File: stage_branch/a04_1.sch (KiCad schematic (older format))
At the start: 17 parts, among them U4001 74HC02, U4002 74HC27, U4003 74LVC07, U4004 74HC27, U4005 74HC02, U4006 74HC02, U4007 74HC04, U4008 74HC04, U4009 74HC27, U4010 74HC4002, U4011 74HC02, U4012 74HC02, U4013 74HC02, U4014 74HC4002, U4015 74HC27

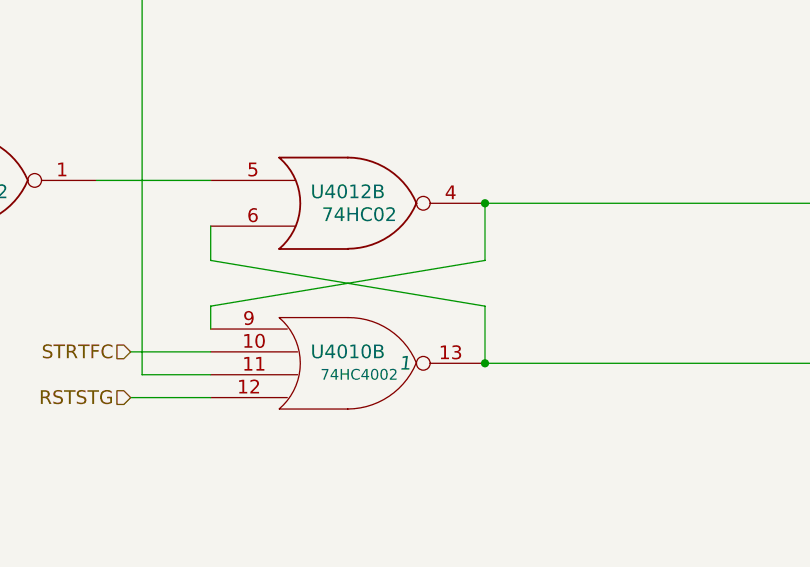
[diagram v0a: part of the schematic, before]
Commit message: More initial conditions fixes, prevents STG3 from oscillating and freqking out TC0
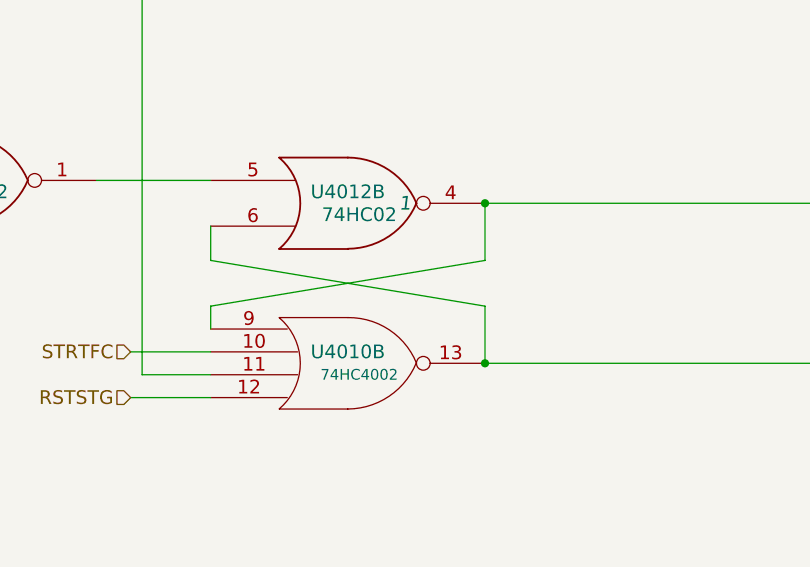
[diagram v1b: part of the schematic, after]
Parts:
- U4010: Initial 1 -> (none)
- U4012: Initial (none) -> 1
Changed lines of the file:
@@
 F 2 "" H 3850 8000 60  0000 C CNN
 F 3 "" H 3850 8000 60  0000 C CNN
-F 4 "1" H 4100 8000 60  0000 C CIN "Initial"
 	2    3850 8000
 	1    0    0    -1
@@
 F 2 "" H 3850 7300 60  0000 C CNN
 F 3 "" H 3850 7300 60  0000 C CNN
+F 4 "1" H 4100 7300 60  0000 C CIN "Initial"
 	2    3850 7300
 	1    0    0    -1

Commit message: Finished off the first page of the Stage Branch Decoding module.
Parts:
- added R2007, R3004, R3005, R4003, R4006: 5k, symbol R
- added unit 5 of U4003
- added unit 6 of U4003
- added unit 4 of U4007
- added unit 5 of U4007
- added unit 5 of U4008
- added unit 6 of U4008
- added unit 3 of U4013
- added unit 4 of U4013
- added unit 2 of U4015
- added unit 3 of U4015
- added U4016, U4018, U4019, U4021, U4024, U4030: 74HC02, symbol 74HC02
- added U4017, U4025: 74HC04, symbol 74HC04
- added U4020, U4026: 74HC27, symbol 74HC27
- added U4022, U4027, U4028: 74HC4002, symbol 74HC4002
- added U4023, U4029: 74LVC07, symbol 74LVC07
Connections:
- net GND: now also U4003.7 (GND), U4003.7 (GND), U4007.7 (GND), U4007.7 (GND), U4008.7 (GND), U4008.7 (GND), U4013.7 (GND), U4013.7 (GND), U4015.7 (GND), U4015.7 (GND), U4016.7 (GND), U4016.7 (GND), U4016.7 (GND), U4016.7 (GND), U4017.7 (GND), U4017.7 (GND), U4017.7 (GND), U4017.7 (GND), U4017.7 (GND), U4017.7 (GND), U4018.7 (GND), U4018.7 (GND), U4018.7 (GND), U4018.7 (GND), U4019.7 (GND), U4019.7 (GND), U4019.7 (GND), U4019.7 (GND), U4020.7 (GND), U4020.7 (GND), U4020.7 (GND), U4021.7 (GND), U4021.7 (GND), U4021.7 (GND), U4021.7 (GND), U4022.7 (GND), U4022.7 (GND), U4023.7 (GND), U4023.7 (GND), U4023.7 (GND), U4023.7 (GND), U4023.7 (GND), U4023.7 (GND), U4024.7 (GND), U4024.7 (GND), U4024.7 (GND), U4024.7 (GND), U4025.7 (GND), U4025.7 (GND), U4025.7 (GND), U4025.7 (GND), U4026.7 (GND), U4026.7 (GND), U4026.7 (GND), U4027.7 (GND), U4027.7 (GND), U4028.7 (GND), U4028.7 (GND), U4029.7 (GND), U4029.7 (GND), U4029.7 (GND), U4029.7 (GND), U4029.7 (GND), U4030.7 (GND), U4030.7 (GND)
- net PHS3/: now also U4019.6, U4021.3, U4021.6, U4022.3, U4024.9, U4030.3
- net ST0/: now also U4018.3
- net ST1/: now also U4018.6
- net ST4/: now also U4018.9
- net STG1: now also U4013.8
- net STG3: now also U4013.9
- net VCC: now also R2007.1, R3004.1, R3005.1, R4003.1, R4006.1, U4003.14 (VCC), U4003.14 (VCC), U4007.14 (VCC), U4007.14 (VCC), U4008.14 (VCC), U4008.14 (VCC), U4013.14 (VCC), U4013.14 (VCC), U4015.14 (VCC), U4015.14 (VCC), U4016.14 (VCC), U4016.14 (VCC), U4016.14 (VCC), U4016.14 (VCC), U4017.14 (VCC), U4017.14 (VCC), U4017.14 (VCC), U4017.14 (VCC), U4017.14 (VCC), U4017.14 (VCC), U4018.14 (VCC), U4018.14 (VCC), U4018.14 (VCC), U4018.14 (VCC), U4019.14 (VCC), U4019.14 (VCC), U4019.14 (VCC), U4019.14 (VCC), U4020.14 (VCC), U4020.14 (VCC), U4020.14 (VCC), U4021.14 (VCC), U4021.14 (VCC), U4021.14 (VCC), U4021.14 (VCC), U4022.14 (VCC), U4022.14 (VCC), U4023.14 (VCC), U4023.14 (VCC), U4023.14 (VCC), U4023.14 (VCC), U4023.14 (VCC), U4023.14 (VCC), U4024.14 (VCC), U4024.14 (VCC), U4024.14 (VCC), U4024.14 (VCC), U4025.14 (VCC), U4025.14 (VCC), U4025.14 (VCC), U4025.14 (VCC), U4026.14 (VCC), U4026.14 (VCC), U4026.14 (VCC), U4027.14 (VCC), U4027.14 (VCC), U4028.14 (VCC), U4028.14 (VCC), U4029.14 (VCC), U4029.14 (VCC), U4029.14 (VCC), U4029.14 (VCC), U4029.14 (VCC), U4030.14 (VCC), U4030.14 (VCC)
- net at U4004.8, U4008.3: now also U4016.8
- net at U4007.3, U4009.10, U4011.10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: now also U4013.11
- net at U4008.9, U4015.12: now also U4016.2
- new net: U4013.10, U4013.12
- new net: U4016.1, U4016.6
- new net: U4015.6, U4017.1
- new net: U4019.1, U4022.2
- new net: U4003.11, U4015.8
- new net: U4003.13, U4019.4
- new net: U4019.10, U4021.12
- new net: U4017.10, U4019.12, U4021.5
- new net: U4019.13, U4020.3
- new net: U4020.12, U4020.4
- new net: U4020.10, U4021.1
- new net: U4020.11, U4021.4
- new net: U4021.10, U4024.2, U4028.12
- new net: U4022.1, U4024.3
- new net: U4021.13, U4023.1
- new net: R3004.2, U4007.9, U4017.13, U4020.9, U4023.2, U4023.4
- new net: R3005.2, U4020.5, U4023.6, U4023.8, U4025.1
- new net: U4020.6, U4023.3
- new net: U4020.8, U4023.5
- new net: U4023.9, U4024.1
- new net: U4026.12, U4030.5
- new net: U4024.4, U4030.6
- new net: U4024.8, U4025.4, U4026.5
- new net: U4026.6, U4026.9
- new net: U4024.10, U4028.10
- new net: U4022.13, U4023.11
- new net: U4023.13, U4027.1
- new net: U4027.13, U4029.1
- new net: U4028.1, U4029.3
- new net: U4024.13, U4029.5
- new net: R4006.2, U4023.10, U4023.12, U4026.10, U4029.2, U4029.4, U4029.6
- new net: U4028.11, U4030.1
- new net: U4025.9, U4026.11, U4028.13
- new net: U4026.8, U4029.11
- new net: U4029.9, U4030.4
- new net: R2007.2, U4007.11, U4025.5, U4028.9, U4029.10, U4029.8
- new net BR1: U4017.12
- new net BR1/: U4025.2
- new net BR2: U4025.6
- new net BR2/: U4025.8
- new net DIV/: U4016.11, U4016.5, U4017.2, U4018.11, U4018.2, U4018.5, U4018.8
- new net DV0: U4017.3, U4018.1
- new net DV0/: U4017.4
- new net DV1: U4017.5, U4018.4
- new net DV1/: U4017.6
- new net DV1376: U4008.13, U4016.13
- new net DV1736/: U4008.12
- new net DV376: U4017.9, U4018.13
- new net DV376/: U4017.8
- new net DV3764: U4016.4
- new net DV4: U4018.10
- new net GEQZRO/: U4026.1
- new net L15/: U4019.11
- new net MBR1: U4007.8
- new net MBR2: U4007.10
- new net OVF/: U4024.6
- new net PHS2/: U4021.9
- new net PHS4: U4019.5, U4022.5
- new net PHS4/: U4020.1, U4024.12, U4026.2, U4026.4
- new net QC0/: U4015.3
- new net SGUM: R4003.2, U4003.10, U4003.12, U4021.11
- new net SQ1/: U4015.5
- new net SQEXT/: U4015.4
- new net ST1376/: U4016.10, U4016.12
- new net ST376: U4008.11, U4013.13, U4016.3, U4016.9
- new net ST376/: U4008.10, U4018.12
- new net SUMA16/: U4015.10, U4019.2
- new net SUMB16/: U4015.9, U4019.3
- new net TL15: U4017.11
- new net TMZ/: U4024.11, U4030.2
- new net TOV/: U4019.9, U4021.8, U4024.5
- new net TPZG/: U4026.13
- new net TSGN/: U4020.13, U4021.2
- new net TSGN2: U4025.3
- new net TSGU/: U4015.11, U4022.4
- new net UNF/: U4019.8
- new net WL01/: U4028.5
- new net WL02/: U4028.4
- new net WL03/: U4028.3
- new net WL04/: U4028.2
- new net WL05/: U4027.12
- new net WL06/: U4027.11
- new net WL07/: U4027.10
- new net WL08/: U4027.9
- new net WL09/: U4027.5
- new net WL10/: U4027.4
- new net WL11/: U4027.3
- new net WL12/: U4027.2
- new net WL13/: U4022.12
- new net WL14/: U4022.11
- new net WL15/: U4022.10
- new net WL16/: U4020.2, U4022.9, U4026.3
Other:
- moved on the sheet: U4001A, U4001B, U4001C, U4002A, U4002B, U4002C, U4004B, U4004C, U4005C, U4005D, U4006A, U4006B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

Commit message: Added page 2 of the Stage Branch Decoding module, and tied it into the rest of the system
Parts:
- added unit 6 of U4007
- added unit 5 of U4025
- added U4058: 74HC04, symbol 74HC04
- renumbered R2007 to R4007
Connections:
- net DV4: now also U4025.11
- net DVST: now also U4007.13
- net GND: now also U4007.7 (GND), U4025.7 (GND), U4058.7 (GND)
- net VCC: now also U4007.14 (VCC), U4025.14 (VCC), U4058.14 (VCC)
- net DVST/: no longer names the net of U4005.5, U4006.11, U4012.2
- net DVST/: now also U4007.12
- net TRSM/: no longer names the net of U4010.2
- net TRSM/: now also U4058.6
- new net DV4/: U4025.10
- new net TRSM: U4058.5
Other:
- moved on the sheet: R4001, R4002, U4001A, U4001B, U4001C, U4001D, U4002A, U4002B, U4002C, U4003A, U4003B, U4003C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

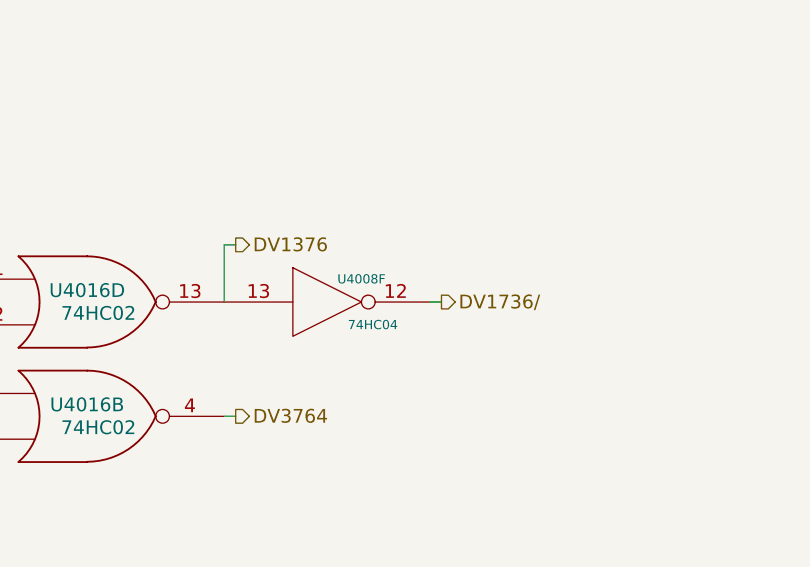
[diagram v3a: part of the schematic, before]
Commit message: Tied in module 6 and corrected a handful of naming/routing errors... most notably some missing gates from A06-1
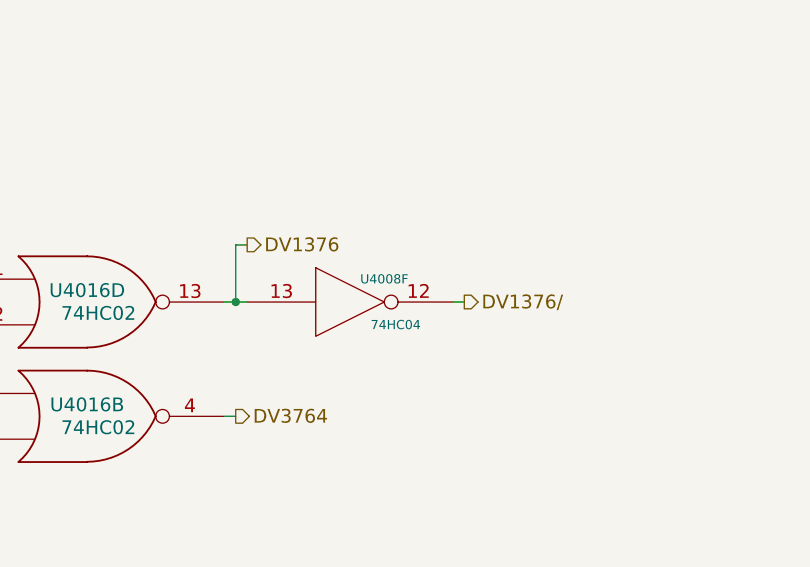
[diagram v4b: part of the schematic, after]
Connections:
- net DV1736/ renamed DV1376/
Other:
- moved on the sheet: U4008F
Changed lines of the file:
@@
 $EndComp
 $Comp
-L VCC #PWR06
+L VCC #PWR05
 U 1 1 56322DE9
 P 6000 2800
-F 0 "#PWR06" H 6000 2650 50  0001 C CNN
+F 0 "#PWR05" H 6000 2650 50  0001 C CNN
 F 1 "VCC" H 6000 2950 50  0000 C CNN
 F 2 "" H 6000 2800 60  0000 C CNN
@@
 $EndComp
 $Comp
-L VCC #PWR07
+L VCC #PWR06
 U 1 1 563274AD
 P 6000 4600
-F 0 "#PWR07" H 6000 4450 50  0001 C CNN
+F 0 "#PWR06" H 6000 4450 50  0001 C CNN
 F 1 "VCC" H 6000 4750 50  0000 C CNN
 F 2 "" H 6000 4600 60  0000 C CNN
@@
 ST1376/
 Wire Wire Line
-	15600 6450 15600 6200
-Wire Wire Line
-	15600 6200 15650 6200
-Text HLabel 15650 6200 2    60   Output ~ 0
+	15650 6450 15650 6200
+Wire Wire Line
+	15650 6200 15700 6200
+Text HLabel 15700 6200 2    60   Output ~ 0
 DV1376
 $Comp
 L 74HC04 U4008
 U 6 1 563B1140
-P 16050 6450
-F 0 "U4008" H 16200 6550 40  0000 C CNN
-F 1 "74HC04" H 16250 6350 40  0000 C CNN
-F 2 "" H 16050 6450 60  0000 C CNN
-F 3 "" H 16050 6450 60  0000 C CNN
-	6    16050 6450
-	1    0    0    -1
-$EndComp
-Wire Wire Line
-	16500 6450 16550 6450
-Text HLabel 16550 6450 2    60   Output ~ 0
-DV1736/
+P 16150 6450
+F 0 "U4008" H 16300 6550 40  0000 C CNN
+F 1 "74HC04" H 16350 6350 40  0000 C CNN
+F 2 "" H 16150 6450 60  0000 C CNN
+F 3 "" H 16150 6450 60  0000 C CNN
+	6    16150 6450
+	1    0    0    -1
+$EndComp
+Wire Wire Line
+	16600 6450 16650 6450
+Text HLabel 16650 6450 2    60   Output ~ 0
+DV1376/
 $Comp
 L 74HC27 U4015
@@
 	6650 10250 6650 10200
 $Comp
-L VCC #PWR08
+L VCC #PWR07
 U 1 1 563E21C1
 P 6650 10200
-F 0 "#PWR08" H 6650 10050 50  0001 C CNN
+F 0 "#PWR07" H 6650 10050 50  0001 C CNN
 F 1 "VCC" H 6650 10350 50  0000 C CNN
 F 2 "" H 6650 10200 60  0000 C CNN
@@
 Connection ~ 9050 12150
 $Comp
-L VCC #PWR09
+L VCC #PWR08
 U 1 1 56428A57
 P 9050 11800
-F 0 "#PWR09" H 9050 11650 50  0001 C CNN
+F 0 "#PWR08" H 9050 11650 50  0001 C CNN
 F 1 "VCC" H 9050 11950 50  0000 C CNN
 F 2 "" H 9050 11800 60  0000 C CNN
@@
 $EndComp
 $Comp
-L VCC #PWR010
+L VCC #PWR09
 U 1 1 56428D13
 P 9100 12900
-F 0 "#PWR010" H 9100 12750 50  0001 C CNN
+F 0 "#PWR09" H 9100 12750 50  0001 C CNN
 F 1 "VCC" H 9100 13050 50  0000 C CNN
 F 2 "" H 9100 12900 60  0000 C CNN
@@
 Connection ~ 15750 11550
 $Comp
-L VCC #PWR011
+L VCC #PWR010
 U 1 1 5644559D
 P 15750 11200
-F 0 "#PWR011" H 15750 11050 50  0001 C CNN
+F 0 "#PWR010" H 15750 11050 50  0001 C CNN
 F 1 "VCC" H 15750 11350 50  0000 C CNN
 F 2 "" H 15750 11200 60  0000 C CNN
@@
 $EndComp
 $Comp
-L VCC #PWR012
+L VCC #PWR011
 U 1 1 56466CE0
 P 18900 11300
-F 0 "#PWR012" H 18900 11150 50  0001 C CNN
+F 0 "#PWR011" H 18900 11150 50  0001 C CNN
 F 1 "VCC" H 18900 11450 50  0000 C CNN
 F 2 "" H 18900 11300 60  0000 C CNN
@@
 Wire Wire Line
 	1750 4950 2150 4950
+Wire Wire Line
+	15600 6450 15700 6450
+Connection ~ 15650 6450
 $EndSCHEMATC
